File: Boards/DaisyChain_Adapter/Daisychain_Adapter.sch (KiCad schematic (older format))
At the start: 3 parts, among them P1 CONN_01X05, P2 CONN_01X05, P3 CONN_01X05

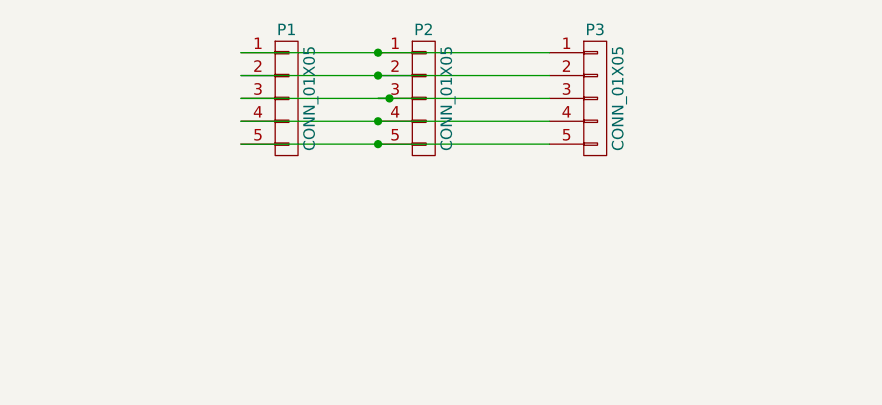
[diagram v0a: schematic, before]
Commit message: Built I2C Daisychain Card
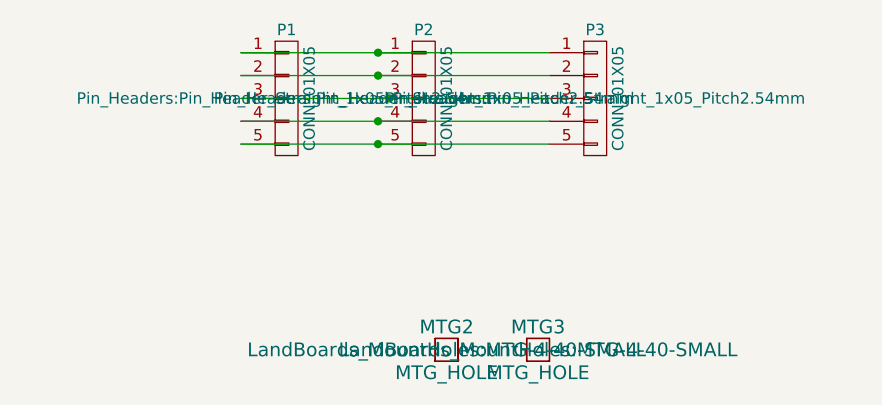
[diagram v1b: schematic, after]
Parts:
- added MTG2, MTG3: MTG_HOLE, LandBoards_MountHoles:MTG-4-40-SMALL, symbol MTG_HOLE
- P1, P2, P3: footprint (none) -> Pin_Headers:Pin_Header_Straight_1x05_Pitch2.54mm
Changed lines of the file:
@@
 EESchema Schematic File Version 2
+LIBS:DougsSch
 LIBS:power
 LIBS:device
@@
 LIBS:74xx
 LIBS:cmos4000
-LIBS:adc-dac
-LIBS:memory
-LIBS:xilinx
-LIBS:microcontrollers
-LIBS:dsp
-LIBS:microchip
-LIBS:analog_switches
-LIBS:motorola
-LIBS:texas
-LIBS:intel
-LIBS:audio
-LIBS:interface
-LIBS:digital-audio
-LIBS:philips
-LIBS:display
-LIBS:cypress
-LIBS:siliconi
-LIBS:opto
-LIBS:atmel
-LIBS:contrib
-LIBS:valves
+LIBS:Daisychain_Adapter-cache
 EELAYER 25 0
 EELAYER END
@@
 F 0 "P1" H 4550 3500 50  0000 C CNN
 F 1 "CONN_01X05" V 4650 3200 50  0000 C CNN
-F 2 "" H 4550 3200 50  0000 C CNN
+F 2 "Pin_Headers:Pin_Header_Straight_1x05_Pitch2.54mm" H 4550 3200 50  0000 C CNN
 F 3 "" H 4550 3200 50  0000 C CNN
 	1    4550 3200
@@
 F 0 "P2" H 5150 3500 50  0000 C CNN
 F 1 "CONN_01X05" V 5250 3200 50  0000 C CNN
-F 2 "" H 5150 3200 50  0000 C CNN
+F 2 "Pin_Headers:Pin_Header_Straight_1x05_Pitch2.54mm" H 5150 3200 50  0000 C CNN
 F 3 "" H 5150 3200 50  0000 C CNN
 	1    5150 3200
@@
 F 0 "P3" H 5900 3500 50  0000 C CNN
 F 1 "CONN_01X05" V 6000 3200 50  0000 C CNN
-F 2 "" H 5900 3200 50  0000 C CNN
+F 2 "Pin_Headers:Pin_Header_Straight_1x05_Pitch2.54mm" H 5900 3200 50  0000 C CNN
 F 3 "" H 5900 3200 50  0000 C CNN
 	1    5900 3200
@@
 Connection ~ 4950 3300
 Connection ~ 4950 3400
+$Comp
+L MTG_HOLE MTG3
+U 1 1 58CF3A4B
+P 5650 4300
+F 0 "MTG3" H 5650 4400 60  0000 C CNN
+F 1 "MTG_HOLE" H 5650 4200 60  0000 C CNN
+F 2 "LandBoards_MountHoles:MTG-4-40-SMALL" H 5650 4300 60  0000 C CNN
+F 3 "" H 5650 4300 60  0000 C CNN
+	1    5650 4300
+	1    0    0    -1
+$EndComp
+$Comp
+L MTG_HOLE MTG2
+U 1 1 58CF3BDC
+P 5250 4300
+F 0 "MTG2" H 5250 4400 60  0000 C CNN
+F 1 "MTG_HOLE" H 5250 4200 60  0000 C CNN
+F 2 "LandBoards_MountHoles:MTG-4-40-SMALL" H 5250 4300 60  0000 C CNN
+F 3 "" H 5250 4300 60  0000 C CNN
+	1    5250 4300
+	1    0    0    -1
+$EndComp
 $EndSCHEMATC
